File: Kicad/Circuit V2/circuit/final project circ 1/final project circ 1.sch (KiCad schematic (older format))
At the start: 55 parts, among them J1 Conn_01x04_Female, J10 Conn_01x02_Female, J11 Conn_01x02_Female, J2 Conn_01x04_Female, J3 USB_B_Micro, J4 Conn_01x04_Female, J5 Conn_01x03_Female, J6 Conn_01x03_Female, J7 Conn_01x04_Female, J8 Conn_01x02_Female, J9 Conn_01x02_Female, SW1 SW_Push, SW2 SW_Push, U1 CP2102N-A01-GQFN28, U2 AZ1117-3.3, U3 AZ1117-3.3, U4 ESP32-WROOM-32D, U5 L2293QTR

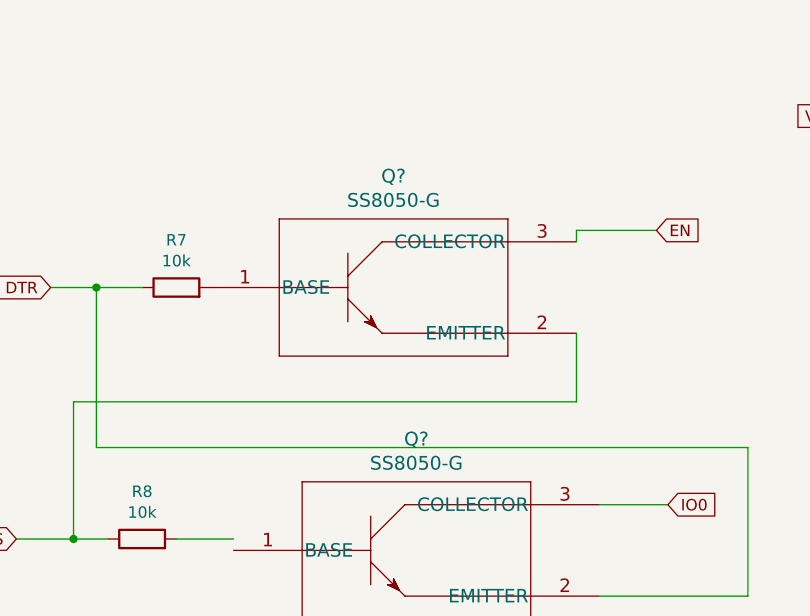
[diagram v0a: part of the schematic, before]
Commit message: updated footprints
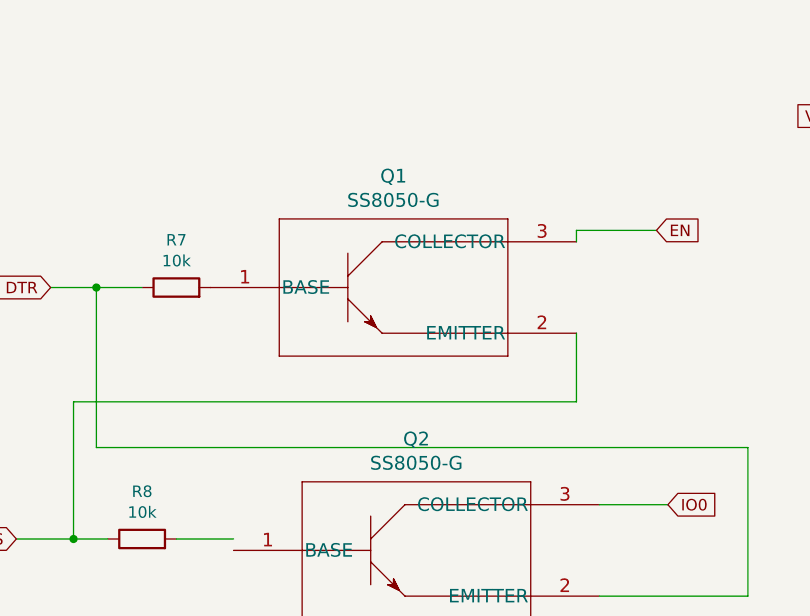
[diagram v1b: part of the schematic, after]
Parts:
- J10, J11, J8, J9: footprint Connector_PinSocket_2.54mm:PinSocket_1x02_P2.54mm_Vertical -> bigboard:button
- J5, J6: footprint Connector_PinSocket_2.54mm:PinSocket_1x03_P2.54mm_Vertical -> bigboard:encoder_out
- Q1, Q2: renamed from Q?; footprint TRAN_SS8050-G_CIP -> bigboard:SS8050-G
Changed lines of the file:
@@
 F 0 "J5" H 29978 15176 50  0000 L CNN
 F 1 "Conn_01x03_Female" H 29978 15085 50  0000 L CNN
-F 2 "Connector_PinSocket_2.54mm:PinSocket_1x03_P2.54mm_Vertical" H 29950 15150 50  0001 C CNN
+F 2 "bigboard:encoder_out" H 29950 15150 50  0001 C CNN
 F 3 "~" H 29950 15150 50  0001 C CNN
 	1    29950 15150
@@
 F 0 "J6" V 29938 16612 50  0000 R CNN
 F 1 "Conn_01x03_Female" V 29847 16612 50  0000 R CNN
-F 2 "Connector_PinSocket_2.54mm:PinSocket_1x03_P2.54mm_Vertical" H 30000 16800 50  0001 C CNN
+F 2 "bigboard:encoder_out" H 30000 16800 50  0001 C CNN
 F 3 "~" H 30000 16800 50  0001 C CNN
 	1    30000 16800
@@
 F 0 "J8" V 33338 14462 50  0000 R CNN
 F 1 "Conn_01x02_Female" V 33247 14462 50  0000 R CNN
-F 2 "Connector_PinSocket_2.54mm:PinSocket_1x02_P2.54mm_Vertical" H 33400 14650 50  0001 C CNN
+F 2 "bigboard:button" H 33400 14650 50  0001 C CNN
 F 3 "~" H 33400 14650 50  0001 C CNN
 	1    33400 14650
@@
 F 0 "J9" V 33338 15112 50  0000 R CNN
 F 1 "Conn_01x02_Female" V 33247 15112 50  0000 R CNN
-F 2 "Connector_PinSocket_2.54mm:PinSocket_1x02_P2.54mm_Vertical" H 33400 15300 50  0001 C CNN
+F 2 "bigboard:button" H 33400 15300 50  0001 C CNN
 F 3 "~" H 33400 15300 50  0001 C CNN
 	1    33400 15300
@@
 F 0 "J10" V 33338 15812 50  0000 R CNN
 F 1 "Conn_01x02_Female" V 33247 15812 50  0000 R CNN
-F 2 "Connector_PinSocket_2.54mm:PinSocket_1x02_P2.54mm_Vertical" H 33400 16000 50  0001 C CNN
+F 2 "bigboard:button" H 33400 16000 50  0001 C CNN
 F 3 "~" H 33400 16000 50  0001 C CNN
 	1    33400 16000
@@
 F 0 "J11" V 33338 16462 50  0000 R CNN
 F 1 "Conn_01x02_Female" V 33247 16462 50  0000 R CNN
-F 2 "Connector_PinSocket_2.54mm:PinSocket_1x02_P2.54mm_Vertical" H 33400 16650 50  0001 C CNN
+F 2 "bigboard:button" H 33400 16650 50  0001 C CNN
 F 3 "~" H 33400 16650 50  0001 C CNN
 	1    33400 16650
@@
 $EndComp
 $Comp
-L Custom:SS8050-G Q?
+L Custom:SS8050-G Q1
 U 1 1 6208535A
 P 15050 14000
-F 0 "Q?" H 15850 14487 60  0000 C CNN
+F 0 "Q1" H 15850 14487 60  0000 C CNN
 F 1 "SS8050-G" H 15850 14381 60  0000 C CNN
-F 2 "TRAN_SS8050-G_CIP" H 15850 14340 60  0001 C CNN
+F 2 "bigboard:SS8050-G" H 15850 14340 60  0001 C CNN
 F 3 "" H 15050 14000 60  0000 C CNN
 	1    15050 14000
@@
 $EndComp
 $Comp
-L Custom:SS8050-G Q?
+L Custom:SS8050-G Q2
 U 1 1 6208695C
 P 15150 15150
-F 0 "Q?" H 15950 15637 60  0000 C CNN
+F 0 "Q2" H 15950 15637 60  0000 C CNN
 F 1 "SS8050-G" H 15950 15531 60  0000 C CNN
-F 2 "TRAN_SS8050-G_CIP" H 15950 15490 60  0001 C CNN
+F 2 "bigboard:SS8050-G" H 15950 15490 60  0001 C CNN
 F 3 "" H 15150 15150 60  0000 C CNN
 	1    15150 15150

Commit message: connected power supply?
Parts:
- added C1: 100p, Capacitor_SMD:C_0402_1005Metric, symbol Device:C
- added C10, C11, C12, C8, C9: 100u, Capacitor_THT:CP_Radial_D6.3mm_P2.50mm, symbol Device:C
- added C13: 1u, Capacitor_THT:CP_Radial_D6.3mm_P2.50mm, symbol Device:C
- added C2: 4.7n, symbol Device:C
- added C3, C4, C6: 0.1u, symbol Device:C
- added C5: 1n, symbol Device:C
- added C7: 4.7u, symbol Device:C
- added D1, D2, D3, D4: 1N4004, Diode_THT:D_DO-41_SOD81_P10.16mm_Horizontal, symbol Diode:1N4004
- added D5: BZT52Bxx, Diode_SMD:D_SOD-123, symbol Diode:BZT52Bxx
- added L1: 33u, SDESIGN:MPXV1D1740L330, symbol Device:L
- added Q1, Q2, Q3: FDD770N15A, Package_TO_SOT_SMD:TO-252-3_TabPin2, symbol SDPowSupply-rescue:FDD770N15A-POWSYMBOLS
- added Q6: 2SC1945, Package_TO_SOT_THT:TO-220-3_Vertical, symbol Transistor_BJT:2SC1945
- added R1, R8: 10k, symbol Device:R
- added R2: 30.1k, symbol Device:R
- added R3: 36.5k, Resistor_SMD:R_0201_0603Metric, symbol Device:R
- added R4: 511k, Resistor_SMD:R_0603_1608Metric, symbol Device:R
- added R5: 6m, Resistor_SMD:R_0805_2012Metric, symbol Device:R
- added U1: LTC3895IFE, SDESIGN:LTC3895IFE, symbol SDPowSupply-rescue:LTC3895IFE-POWSYMBOLS
- renumbered C3 to C14, C4 to C15, C5 to C16, C6 to C17, C2 to C18, C7 to C19, C8 to C20, C9 to C21, C10 to C22, C11 to C23, C1 to C24, D1 to D6, D2 to D7, D3 to D8, D4 to D9, J3 to J1, J4 to J2, J1 to J3, J2 to J4, Q1 to Q4, Q2 to Q5, R2 to R10, R9 to R11, R3 to R12, R4 to R13, R6 to R14, R5 to R15, R10 to R16, R11 to R17, R12 to R18, R13 to R19, R14 to R20, R15 to R21, R16 to R22, R17 to R23, R18 to R24, R8 to R6, R1 to R9, U1 to U2, U2 to U3, U5 to U4, U3 to U5, U4 to U6
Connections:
- net labels added: +VDC, LINE, NEUT
- wire segments 235 -> 331
- no-connect marks 0 -> 8
